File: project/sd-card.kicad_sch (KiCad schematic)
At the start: 7 parts, among them J6 Micro_SD_Card_Det2, U4 EMIF06-MSD02N16

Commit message: schemtic is done, need to go through BOM
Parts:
- C117: renamed from C106; value 10u -> 10uF; Manufacturer_Name (none) -> Murata Electronics
- J1: renamed from J6; Manufacturer_Name (none) -> Hirose Electric Co Ltd; Manufacturer_Part_Number (none) -> DM3AT-SF-PEJM5
- R26: renamed from R24; Manufacturer_Name (none) -> YAGEO
- R27: renamed from R25; Manufacturer_Name (none) -> YAGEO
- R28: renamed from R26; Manufacturer_Name (none) -> YAGEO
- U5: renamed from U4; Manufacturer_Name (none) -> STMicroelectronics
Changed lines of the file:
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@@
 		(dnp no)
 		(fields_autoplaced yes)
-		(property "Reference" "#PWR0113"
+		(property "Reference" "#PWR0107"
 			(at 207.01 107.95 0)
 			(effects
@@
 			(project "project"
 				(path "/7afeae28-8837-445b-b53a-5d89eb16eb45/4209e974-b600-4026-b260-5c80dc020876"
-					(reference "#PWR0113")
+					(reference "#PWR0107")
 					(unit 1)
 				)
@@
 		(on_board yes)
 		(dnp no)
-		(property "Reference" "R26"
+		(property "Reference" "R28"
 			(at 156.21 99.06 90)
 			(effects
@@
 		)
 		(property "3DMODEL" ""
+			(at 156.21 105.41 90)
+			(effects
+				(font
+					(size 1.27 1.27)
+				)
+				(hide yes)
+			)
+		)
+		(property "Manufacturer_Name" "YAGEO"
 			(at 156.21 105.41 90)
 			(effects
@@
 			(project "project"
 				(path "/7afeae28-8837-445b-b53a-5d89eb16eb45/4209e974-b600-4026-b260-5c80dc020876"
-					(reference "R26")
+					(reference "R28")
 					(unit 1)
 				)
@@
 		(dnp no)
 		(fields_autoplaced yes)
-		(property "Reference" "#PWR093"
+		(property "Reference" "#PWR0110"
 			(at 160.02 130.81 0)
 			(effects
@@
 			(project "project"
 				(path "/7afeae28-8837-445b-b53a-5d89eb16eb45/4209e974-b600-4026-b260-5c80dc020876"
-					(reference "#PWR093")
+					(reference "#PWR0110")
 					(unit 1)
 				)
@@
 		(dnp no)
 		(fields_autoplaced yes)
-		(property "Reference" "#PWR091"
+		(property "Reference" "#PWR0108"
 			(at 107.95 110.49 0)
 			(effects
@@
 			(project "project"
 				(path "/7afeae28-8837-445b-b53a-5d89eb16eb45/4209e974-b600-4026-b260-5c80dc020876"
-					(reference "#PWR091")
+					(reference "#PWR0108")
 					(unit 1)
 				)
@@
 		(dnp no)
 		(fields_autoplaced yes)
-		(property "Reference" "#PWR089"
+		(property "Reference" "#PWR0104"
 			(at 157.48 91.44 0)
 			(effects
@@
 			(project "project"
 				(path "/7afeae28-8837-445b-b53a-5d89eb16eb45/4209e974-b600-4026-b260-5c80dc020876"
-					(reference "#PWR089")
+					(reference "#PWR0104")
 					(unit 1)
 				)
@@
 		(dnp no)
 		(fields_autoplaced yes)
-		(property "Reference" "#PWR0114"
+		(property "Reference" "#PWR0106"
 			(at 157.48 99.06 0)
 			(effects
@@
 			(project "project"
 				(path "/7afeae28-8837-445b-b53a-5d89eb16eb45/4209e974-b600-4026-b260-5c80dc020876"
-					(reference "#PWR0114")
+					(reference "#PWR0106")
 					(unit 1)
 				)
@@
 		(dnp no)
 		(fields_autoplaced yes)
-		(property "Reference" "#PWR092"
+		(property "Reference" "#PWR0109"
 			(at 138.43 124.46 0)
 			(effects
@@
 			(project "project"
 				(path "/7afeae28-8837-445b-b53a-5d89eb16eb45/4209e974-b600-4026-b260-5c80dc020876"
-					(reference "#PWR092")
+					(reference "#PWR0109")
 					(unit 1)
 				)
@@
 		(dnp no)
 		(fields_autoplaced yes)
-		(property "Reference" "U4"
+		(property "Reference" "U5"
 			(at 108.585 66.04 0)
 			(effects
@@
 		)
 		(property "Manufacturer_Part_Number" "EMIF06-MSD02N16"
+			(at 87.63 78.74 0)
+			(effects
+				(font
+					(size 1.27 1.27)
+				)
+				(hide yes)
+			)
+		)
+		(property "Manufacturer_Name" "STMicroelectronics"
 			(at 87.63 78.74 0)
 			(effects
@@
 			(project "project"
 				(path "/7afeae28-8837-445b-b53a-5d89eb16eb45/4209e974-b600-4026-b260-5c80dc020876"
-					(reference "U4")
+					(reference "U5")
 					(unit 1)
 				)
@@
 		(on_board yes)
 		(dnp no)
-		(property "Reference" "R24"
+		(property "Reference" "R26"
 			(at 71.12 78.7399 0)
 			(effects
@@
 		)
 		(property "3DMODEL" ""
+			(at 73.66 80.01 0)
+			(effects
+				(font
+					(size 1.27 1.27)
+				)
+				(hide yes)
+			)
+		)
+		(property "Manufacturer_Name" "YAGEO"
 			(at 73.66 80.01 0)
 			(effects
@@
 			(project "project"
 				(path "/7afeae28-8837-445b-b53a-5d89eb16eb45/4209e974-b600-4026-b260-5c80dc020876"
-					(reference "R24")
+					(reference "R26")
 					(unit 1)
 				)
@@
 		(dnp no)
 		(fields_autoplaced yes)
-		(property "Reference" "C106"
+		(property "Reference" "C117"
 			(at 142.24 113.0299 0)
 			(effects
@@
 			)
 		)
-		(property "Value" "10u"
+		(property "Value" "10uF"
 			(at 142.24 115.5699 0)
 			(effects
@@
 		)
 		(property "3DMODEL" ""
+			(at 138.43 114.3 0)
+			(effects
+				(font
+					(size 1.27 1.27)
+				)
+				(hide yes)
+			)
+		)
+		(property "Manufacturer_Name" "Murata Electronics"
 			(at 138.43 114.3 0)
 			(effects
@@
 			(project "project"
 				(path "/7afeae28-8837-445b-b53a-5d89eb16eb45/4209e974-b600-4026-b260-5c80dc020876"
-					(reference "C106")
+					(reference "C117")
 					(unit 1)
 				)
@@
 		(on_board yes)
 		(dnp no)
-		(property "Reference" "R25"
+		(property "Reference" "R27"
 			(at 71.12 92.7099 0)
 			(effects
@@
 		)
 		(property "3DMODEL" ""
+			(at 73.66 93.98 0)
+			(effects
+				(font
+					(size 1.27 1.27)
+				)
+				(hide yes)
+			)
+		)
+		(property "Manufacturer_Name" "YAGEO"
 			(at 73.66 93.98 0)
 			(effects
@@
 			(project "project"
 				(path "/7afeae28-8837-445b-b53a-5d89eb16eb45/4209e974-b600-4026-b260-5c80dc020876"
-					(reference "R25")
+					(reference "R27")
 					(unit 1)
 				)
@@
 		(dnp no)
 		(fields_autoplaced yes)
-		(property "Reference" "J6"
+		(property "Reference" "J1"
 			(at 187.325 67.31 0)
 			(effects
@@
 		)
 		(property "Description" "Micro SD Card Socket with two card detection pins"
+			(at 186.69 88.9 0)
+			(effects
+				(font
+					(size 1.27 1.27)
+				)
+				(hide yes)
+			)
+		)
+		(property "Manufacturer_Name" "Hirose Electric Co Ltd"
+			(at 186.69 88.9 0)
+			(effects
+				(font
+					(size 1.27 1.27)
+				)
+				(hide yes)
+			)
+		)
+		(property "Manufacturer_Part_Number" "DM3AT-SF-PEJM5"
 			(at 186.69 88.9 0)
 			(effects
@@
 			(project "project"
 				(path "/7afeae28-8837-445b-b53a-5d89eb16eb45/4209e974-b600-4026-b260-5c80dc020876"
-					(reference "J6")
+					(reference "J1")
 					(unit 1)
 				)
@@
 		(dnp no)
 		(fields_autoplaced yes)
-		(property "Reference" "#PWR090"
+		(property "Reference" "#PWR0105"
 			(at 73.66 104.14 0)
 			(effects
@@
 			(project "project"
 				(path "/7afeae28-8837-445b-b53a-5d89eb16eb45/4209e974-b600-4026-b260-5c80dc020876"
-					(reference "#PWR090")
+					(reference "#PWR0105")
 					(unit 1)
 				)

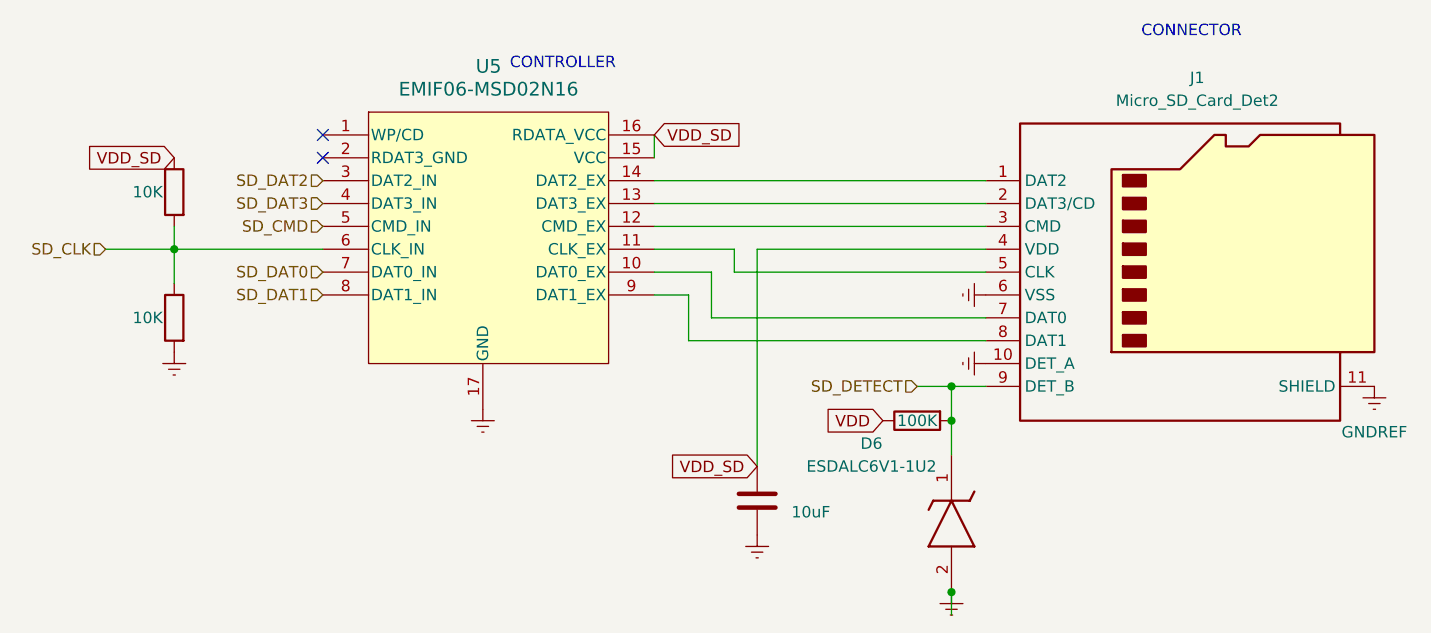
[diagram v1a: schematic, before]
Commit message: schemtic is done, annotation set
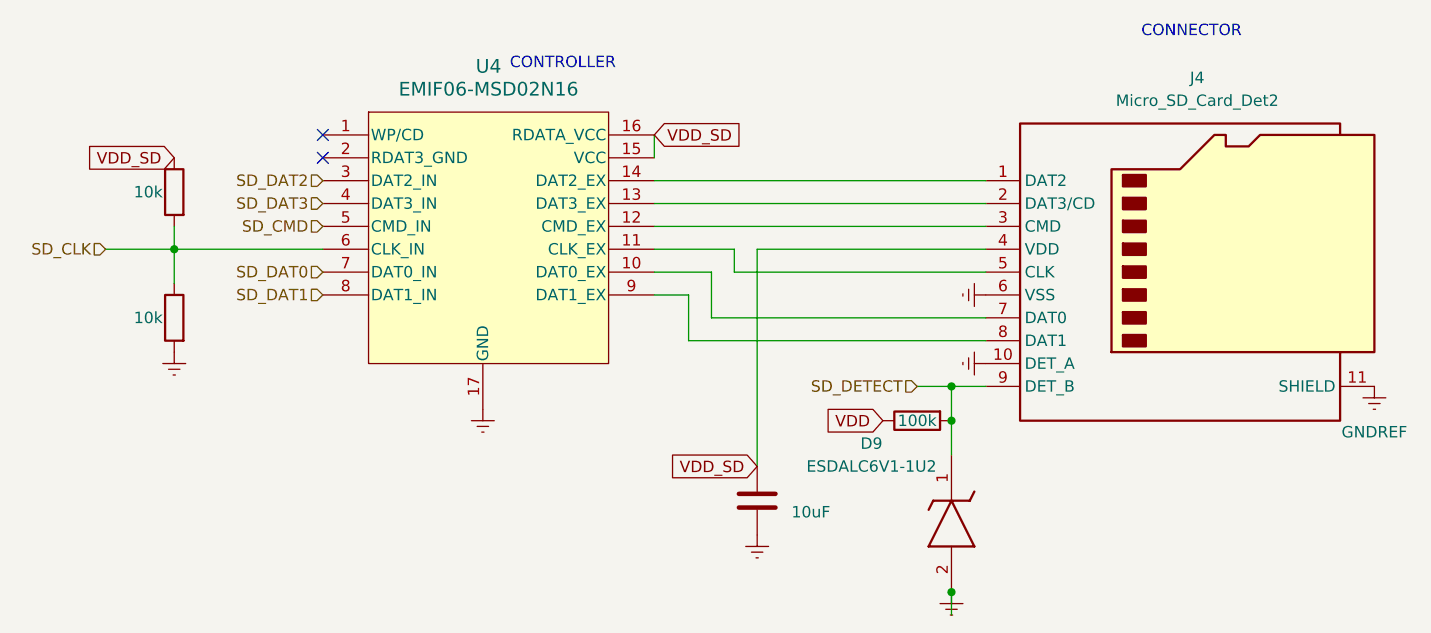
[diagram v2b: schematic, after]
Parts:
- R59: renamed from R26; value 10K -> 10k
- R60: renamed from R27; value 10K -> 10k
- R61: renamed from R28; value 100K -> 100k
- renumbered C117 to C120, D6 to D9, J1 to J4, U5 to U4
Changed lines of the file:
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@@
 		(dnp no)
 		(fields_autoplaced yes)
-		(property "Reference" "#PWR0107"
+		(property "Reference" "#PWR0125"
 			(at 207.01 107.95 0)
 			(effects
@@
 			(project "project"
 				(path "/7afeae28-8837-445b-b53a-5d89eb16eb45/4209e974-b600-4026-b260-5c80dc020876"
-					(reference "#PWR0107")
+					(reference "#PWR0125")
 					(unit 1)
 				)
@@
 		(on_board yes)
 		(dnp no)
-		(property "Reference" "R28"
+		(property "Reference" "R61"
 			(at 156.21 99.06 90)
 			(effects
@@
 			)
 		)
-		(property "Value" "100K"
+		(property "Value" "100k"
 			(at 156.21 105.41 90)
 			(effects
@@
 			(project "project"
 				(path "/7afeae28-8837-445b-b53a-5d89eb16eb45/4209e974-b600-4026-b260-5c80dc020876"
-					(reference "R28")
+					(reference "R61")
 					(unit 1)
 				)
@@
 		(dnp no)
 		(fields_autoplaced yes)
-		(property "Reference" "#PWR0110"
+		(property "Reference" "#PWR0128"
 			(at 160.02 130.81 0)
 			(effects
@@
 			(project "project"
 				(path "/7afeae28-8837-445b-b53a-5d89eb16eb45/4209e974-b600-4026-b260-5c80dc020876"
-					(reference "#PWR0110")
+					(reference "#PWR0128")
 					(unit 1)
 				)
@@
 		(dnp no)
 		(fields_autoplaced yes)
-		(property "Reference" "#PWR0108"
+		(property "Reference" "#PWR0126"
 			(at 107.95 110.49 0)
 			(effects
@@
 			(project "project"
 				(path "/7afeae28-8837-445b-b53a-5d89eb16eb45/4209e974-b600-4026-b260-5c80dc020876"
-					(reference "#PWR0108")
+					(reference "#PWR0126")
 					(unit 1)
 				)
@@
 		(dnp no)
 		(fields_autoplaced yes)
-		(property "Reference" "#PWR0104"
+		(property "Reference" "#PWR0122"
 			(at 157.48 91.44 0)
 			(effects
@@
 			(project "project"
 				(path "/7afeae28-8837-445b-b53a-5d89eb16eb45/4209e974-b600-4026-b260-5c80dc020876"
-					(reference "#PWR0104")
+					(reference "#PWR0122")
 					(unit 1)
 				)
@@
 		(dnp no)
 		(fields_autoplaced yes)
-		(property "Reference" "#PWR0106"
+		(property "Reference" "#PWR0124"
 			(at 157.48 99.06 0)
 			(effects
@@
 			(project "project"
 				(path "/7afeae28-8837-445b-b53a-5d89eb16eb45/4209e974-b600-4026-b260-5c80dc020876"
-					(reference "#PWR0106")
+					(reference "#PWR0124")
 					(unit 1)
 				)
@@
 		(on_board yes)
 		(dnp no)
-		(property "Reference" "D6"
+		(property "Reference" "D9"
 			(at 151.13 107.95 90)
 			(effects
@@
 			(project "project"
 				(path "/7afeae28-8837-445b-b53a-5d89eb16eb45/4209e974-b600-4026-b260-5c80dc020876"
-					(reference "D6")
+					(reference "D9")
 					(unit 1)
 				)
@@
 		(dnp no)
 		(fields_autoplaced yes)
-		(property "Reference" "#PWR0109"
+		(property "Reference" "#PWR0127"
 			(at 138.43 124.46 0)
 			(effects
@@
 			(project "project"
 				(path "/7afeae28-8837-445b-b53a-5d89eb16eb45/4209e974-b600-4026-b260-5c80dc020876"
-					(reference "#PWR0109")
+					(reference "#PWR0127")
 					(unit 1)
 				)
@@
 		(dnp no)
 		(fields_autoplaced yes)
-		(property "Reference" "U5"
+		(property "Reference" "U4"
 			(at 108.585 66.04 0)
 			(effects
@@
 			(project "project"
 				(path "/7afeae28-8837-445b-b53a-5d89eb16eb45/4209e974-b600-4026-b260-5c80dc020876"
-					(reference "U5")
+					(reference "U4")
 					(unit 1)
 				)
@@
 		(on_board yes)
 		(dnp no)
-		(property "Reference" "R26"
+		(property "Reference" "R59"
 			(at 71.12 78.7399 0)
 			(effects
@@
 			)
 		)
-		(property "Value" "10K"
+		(property "Value" "10k"
 			(at 72.39 80.01 0)
 			(effects
@@
 			(project "project"
 				(path "/7afeae28-8837-445b-b53a-5d89eb16eb45/4209e974-b600-4026-b260-5c80dc020876"
-					(reference "R26")
+					(reference "R59")
 					(unit 1)
 				)
@@
 		(dnp no)
 		(fields_autoplaced yes)
-		(property "Reference" "C117"
+		(property "Reference" "C120"
 			(at 142.24 113.0299 0)
 			(effects
@@
 			(project "project"
 				(path "/7afeae28-8837-445b-b53a-5d89eb16eb45/4209e974-b600-4026-b260-5c80dc020876"
-					(reference "C117")
+					(reference "C120")
 					(unit 1)
 				)
@@
 		(on_board yes)
 		(dnp no)
-		(property "Reference" "R27"
+		(property "Reference" "R60"
 			(at 71.12 92.7099 0)
 			(effects
@@
 			)
 		)
-		(property "Value" "10K"
+		(property "Value" "10k"
 			(at 72.39 93.98 0)
 			(effects
@@
 			(project "project"
 				(path "/7afeae28-8837-445b-b53a-5d89eb16eb45/4209e974-b600-4026-b260-5c80dc020876"
-					(reference "R27")
+					(reference "R60")
 					(unit 1)
 				)
@@
 		(dnp no)
 		(fields_autoplaced yes)
-		(property "Reference" "J1"
+		(property "Reference" "J4"
 			(at 187.325 67.31 0)
 			(effects
@@
 			(project "project"
 				(path "/7afeae28-8837-445b-b53a-5d89eb16eb45/4209e974-b600-4026-b260-5c80dc020876"
-					(reference "J1")
+					(reference "J4")
 					(unit 1)
 				)
@@
 		(dnp no)
 		(fields_autoplaced yes)
-		(property "Reference" "#PWR0105"
+		(property "Reference" "#PWR0123"
 			(at 73.66 104.14 0)
 			(effects
@@
 			(project "project"
 				(path "/7afeae28-8837-445b-b53a-5d89eb16eb45/4209e974-b600-4026-b260-5c80dc020876"
-					(reference "#PWR0105")
+					(reference "#PWR0123")
 					(unit 1)
 				)
